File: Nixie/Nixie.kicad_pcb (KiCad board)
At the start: 2 copper layers, 41 parts, among them J1 Conn_01x05_Male, J2 USB_B_Micro, Q1 BC847, Q2 BC847, SW1 SW_Push, U1 K155ID1, U2 ESP-12E, U3 74HC595, U4 K155ID1, U5 K155ID1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

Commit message: Platinenlayout begonnen
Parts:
- moved C1 60.8 mm to (109.2, 65.8), turned to 90 degrees
- moved C7 60.2 mm to (147.7, 126.0), turned to -90 degrees
- moved H4 53.7 mm to (36.8, 49.5)
- moved U7 50.7 mm to (137.5, 120.9), turned to 90 degrees
- moved U4 50.5 mm to (110.5, 120.9), turned to 90 degrees
- moved U1 48.9 mm to (119.5, 70.9), turned to -90 degrees
- moved U5 48.7 mm to (146.5, 70.9), turned to -90 degrees
- moved U9 42.6 mm to (194.7, 93.1), turned to 90 degrees
- moved C10 31.0 mm to (209.1, 100.1)
- moved C5 24.3 mm to (120.7, 126.0), turned to -90 degrees
- moved C4 22.2 mm to (136.5, 65.8)
- moved U8 16.9 mm to (215.6, 92.2), turned to 180 degrees
- moved U3 15.0 mm to (81.5, 95.0), turned to 180 degrees
- moved C9 14.9 mm to (217.6, 100.1), turned to 180 degrees
- moved Q1 14.4 mm to (75.7, 86.2)
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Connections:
- J1 pad 1: /RX -> /TX
- J1 pad 2: /TX -> /RX
- J1 pad 3: /DTR -> /RTS
- J1 pad 4: /RTS -> /DTR
- U1 pad 12: (no net) -> GND
- U4 pad 12: (no net) -> GND
- U5 pad 12: (no net) -> GND
- U7 pad 12: (no net) -> GND
- U9 pad 3: GND -> 170V
- U9 pad 4: 170V -> GND
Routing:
- net Net-(U3-Pad5): track 0.00 -> 74.6 mm
- net Net-(U3-Pad6): track 0.00 -> 67.7 mm, vias 0 -> 1
- net Net-(U3-Pad7): track 0.00 -> 65.2 mm, vias 0 -> 1
- net Net-(U3-Pad15): track 0.00 -> 65.0 mm
- net RST: track 0.00 -> 63.5 mm, vias 0 -> 2
- net Net-(N4-Pad8): track 0.00 -> 60.0 mm
- net Net-(N4-Pad9): track 0.00 -> 57.7 mm, vias 0 -> 1
- net Net-(N3-Pad2): track 0.00 -> 56.3 mm
- net Net-(N2-Pad9): track 0.00 -> 56.1 mm
- net Net-(N1-Pad2): track 0.00 -> 55.3 mm
- net Net-(U3-Pad3): track 0.00 -> 54.9 mm, vias 0 -> 1
- net SER: track 0.00 -> 51.9 mm
- net Net-(N4-Pad0): track 0.00 -> 51.5 mm
- net Net-(N2-Pad8): track 0.00 -> 50.1 mm
- net RCLK: track 0.00 -> 50.0 mm
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
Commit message: PCB fertiggestellt
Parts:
- removed H1, H2: MountingHole_Pad, MountingHole:MountingHole_3.2mm_M3_Pad
- added ?: , , F.Cu at (184.0, 127.0)
- added H4: MountingHole_Pad, MountingHole:MountingHole_3.2mm_M3_Pad, F.Cu at (183.9, 59.9)
- C1, C2, C3, C4, C5, C6, C8: moved to B.Cu
- moved H3 193.9 mm to (64.7, 125.7)
- moved C10 44.3 mm to (169.3, 119.6)
- moved L1 44.3 mm to (169.3, 105.0)
- moved C9 44.3 mm to (177.9, 119.6)
- moved D1 44.3 mm to (174.4, 105.0)
- moved U8 44.3 mm to (175.9, 111.7)
- moved J2 43.4 mm to (186.3, 112.9)
- moved U9 33.1 mm to (167.6, 74.2), turned to 180 degrees
- moved H4 26.7 mm to (61.4, 59.9), turned to 90 degrees
- moved SW1 23.8 mm to (68.3, 103.2), turned to 0 degrees
- moved R2 17.7 mm to (61.5, 94.4)
- moved R1 16.9 mm to (61.8, 102.8), turned to -90 degrees
- moved U2 16.2 mm to (61.4, 81.5)
- moved R5 15.6 mm to (71.4, 70.8)
- moved C2 15.2 mm to (69.3, 95.7)
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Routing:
- net GND: track 13.7 -> 516.5 mm, vias 0 -> 8
- net +5V: track 18.7 -> 256.7 mm, vias 0 -> 3
- net +3.3V: track 17.3 -> 173.6 mm, vias 0 -> 2
- net SR_CLK: track 47.4 -> 198.2 mm, vias 0 -> 2
- net RCLK: track 50.0 -> 198.8 mm, vias 0 -> 2
- net Net-(U3-Pad9): track 0.00 -> 130.3 mm, vias 0 -> 2
- net Net-(U6-Pad7): track 0.00 -> 49.0 mm, vias 0 -> 1
- net Net-(U6-Pad2): track 0.00 -> 48.5 mm, vias 0 -> 1
- net Net-(U6-Pad4): track 0.00 -> 48.5 mm
- net Net-(U6-Pad1): track 0.00 -> 47.3 mm, vias 0 -> 1
- net Net-(U6-Pad3): track 0.00 -> 41.9 mm, vias 0 -> 1
- net Net-(U6-Pad5): track 0.00 -> 39.5 mm, vias 0 -> 1
- net Net-(U6-Pad15): track 0.00 -> 38.9 mm, vias 0 -> 1
- net Net-(U6-Pad6): track 0.00 -> 37.6 mm, vias 0 -> 1
- net Net-(N4-Pad4): track 43.0 -> 14.7 mm
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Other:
- board outline added: 132.3 x 76.6 mm
- copper layers 2 -> 4

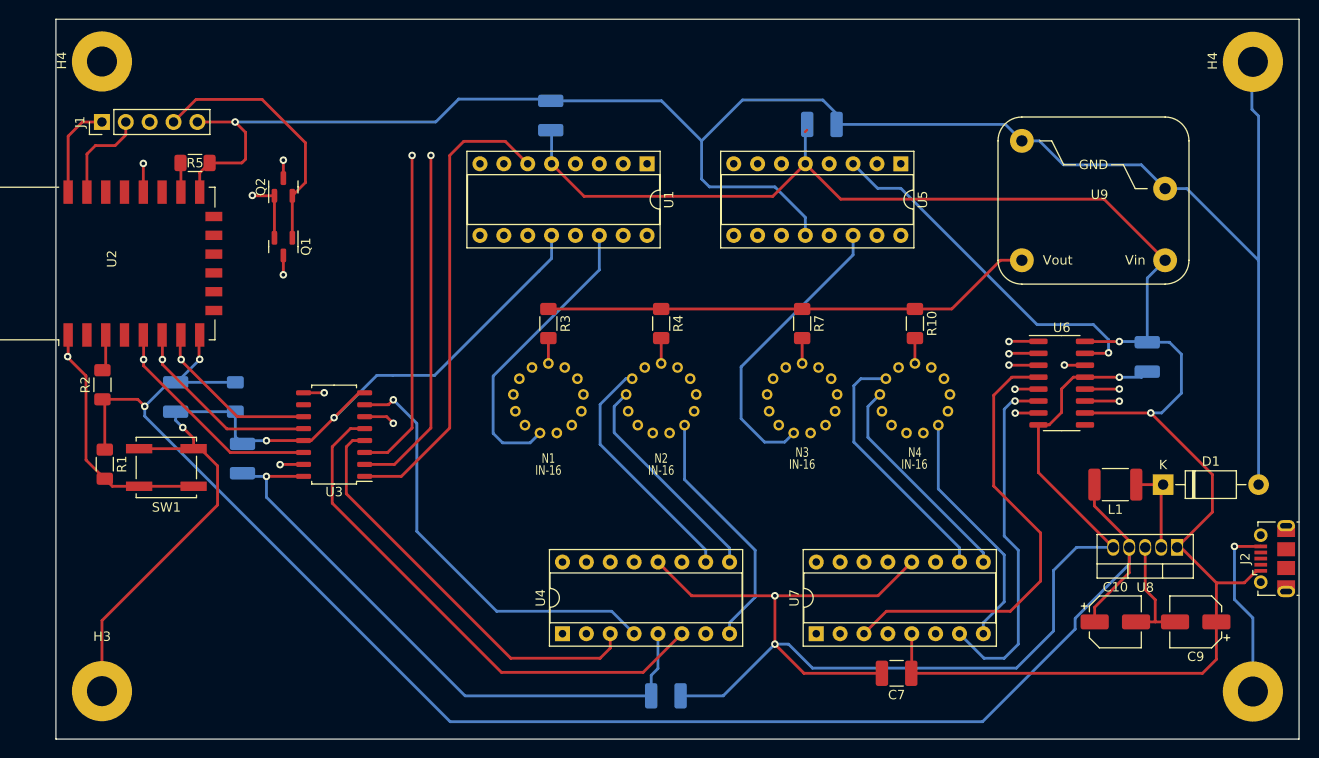
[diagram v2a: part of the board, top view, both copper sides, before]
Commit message: Added solid ground planes
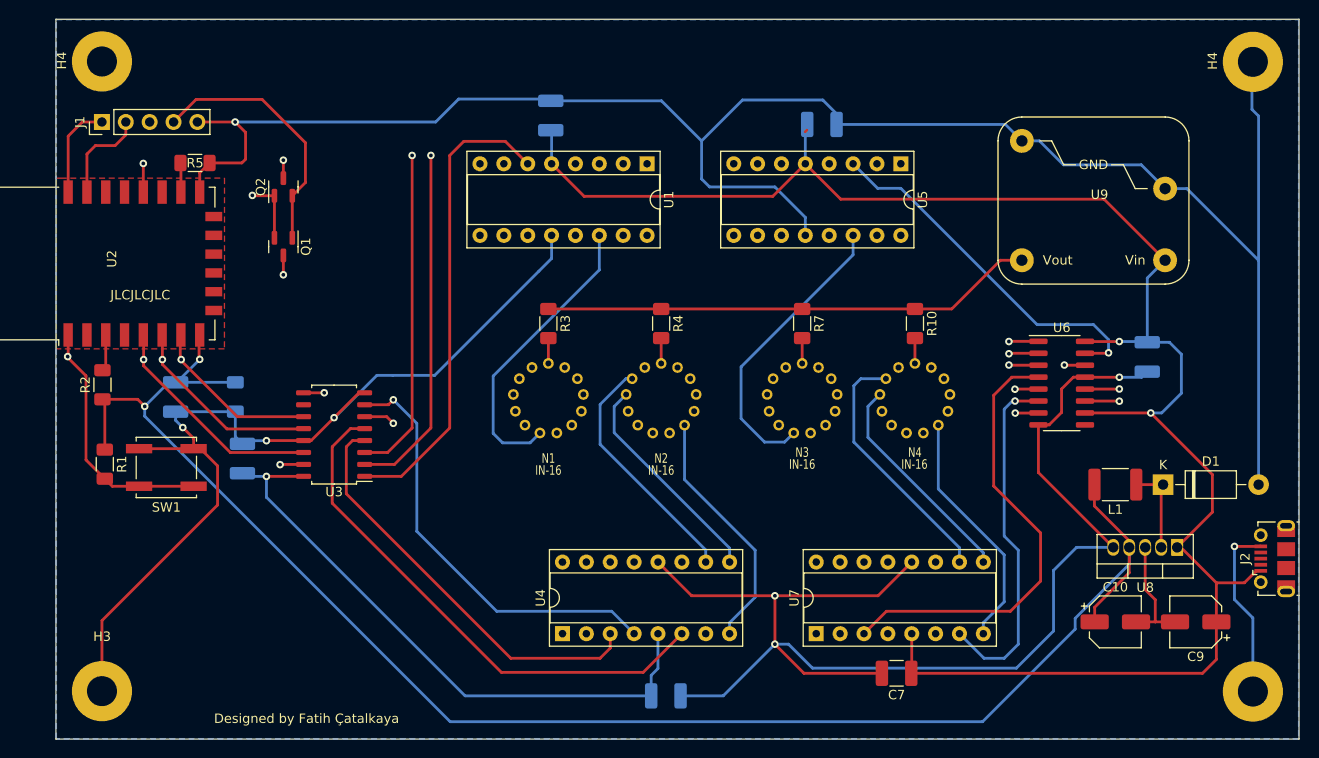
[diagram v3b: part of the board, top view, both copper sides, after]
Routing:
- added copper zone on B.Cu, net GND
- added copper zone on F.Cu, net GND
- added copper zone on In1.Cu, net GND
- added copper zone on In2.Cu, net GND
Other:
- board text added: "Designed by Fatih Çatalkaya"
- board text added: "JLCJLCJLC"
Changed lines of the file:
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@@
   )
   (gr_rect (start 56.6 55.51) (end 188.87 132.1) (layer "Edge.Cuts") (width 0.1) (fill none))
+  (gr_text "JLCJLCJLC\n" (at 65.58 84.85) (layer "F.SilkS")
+    (effects (font (size 1 1) (thickness 0.15)))
+  )
+  (gr_text "Designed by Fatih Çatalkaya" (at 83.27 129.92) (layer "F.SilkS")
+    (effects (font (size 1 1) (thickness 0.15)))
+  )
+  (dimension (type aligned) (layer "Cmts.User")
+    (pts (xy 188.87 55.51) (xy 188.87 132.1))
+    (height -5.13)
+    (gr_text "76.5900 mm" (at 192.85 93.805 90) (layer "Cmts.User")
+      (effects (font (size 1 1) (thickness 0.15)))
+    )
+    (format (units 3) (units_format 1) (precision 4))
+    (style (thickness 0.15) (arrow_length 1.27) (text_position_mode 0) (extension_height 0.58642) (extension_offset 0.5) keep_text_aligned)
+  )
+  (dimension (type aligned) (layer "Cmts.User")
+    (pts (xy 188.87 55.51) (xy 56.6 55.51))
+    (height 3.409999)
+    (gr_text "132.2700 mm" (at 122.735 50.950001) (layer "Cmts.User")
+      (effects (font (size 1 1) (thickness 0.15)))
+    )
+    (format (units 3) (units_format 1) (precision 4))
+    (style (thickness 0.15) (arrow_length 1.27) (text_position_mode 0) (extension_height 0.58642) (extension_offset 0.5) keep_text_aligned)
+  )
   (segment (start 179.65 107.95) (end 179.65 103.95) (width 0.3) (layer "F.Cu") (net 1))
   (segment (start 173.1 97.4) (end 166.095 97.4) (width 0.3) (layer "F.Cu") (net 1))
@@
   (segment (start 157.8 89.8) (end 158 89.8) (width 0.3) (layer "In2.Cu") (net 101))
   (segment (start 138.185 66.5) (end 149 66.5) (width 0.3) (layer "In2.Cu") (net 101))
+  (zone (net 2) (net_name "GND") (layers "F.Cu" "In1.Cu" "In2.Cu") (hatch edge 0.508)
+    (connect_pads (clearance 0.508))
+    (min_thickness 0.254) (filled_areas_thickness no)
+    (fill yes (thermal_gap 0.508) (thermal_bridge_width 0.508))
+    (polygon
+      (pts
+        (xy 74.53 90.58)
+        (xy 56.65 90.58)
+        (xy 56.65 72.42)
+        (xy 57.11 72.42)
+        (xy 74.54 72.41)
+      )
+    )
+  )
+  (zone (net 2) (net_name "GND") (layer "B.Cu") (hatch edge 0.508)
+    (connect_pads (clearance 0.508))
+    (min_thickness 0.254) (filled_areas_thickness no)
+    (fill yes (thermal_gap 0.508) (thermal_bridge_width 0.508))
+    (polygon
+      (pts
+        (xy 188.82 132.05)
+        (xy 56.65 132.05)
+        (xy 56.65 55.56)
+        (xy 188.82 55.56)
+      )
+    )
+  )
 )

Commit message: Kleinere Anpassungen
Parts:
- renumbered H4 to H2
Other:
- board text added: "12.07.2022"
- board text added: "DTR"
- board text added: "GND"
- board text added: "JLCJLCJLCJLC"
- board text added: "RTS"
- board text added: "RX"
- board text added: "TX"
- board text removed: "JLCJLCJLC"

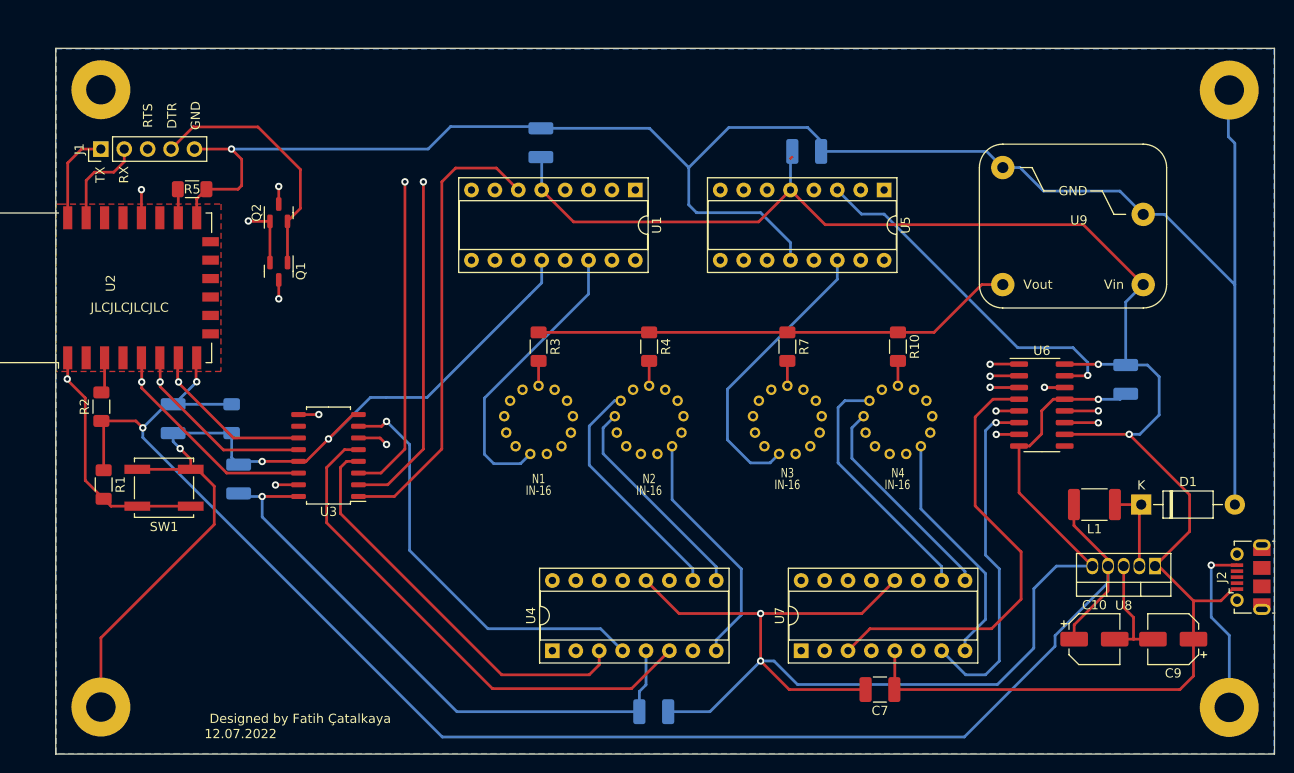
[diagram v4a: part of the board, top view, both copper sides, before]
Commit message: Designed 2-layer PCB
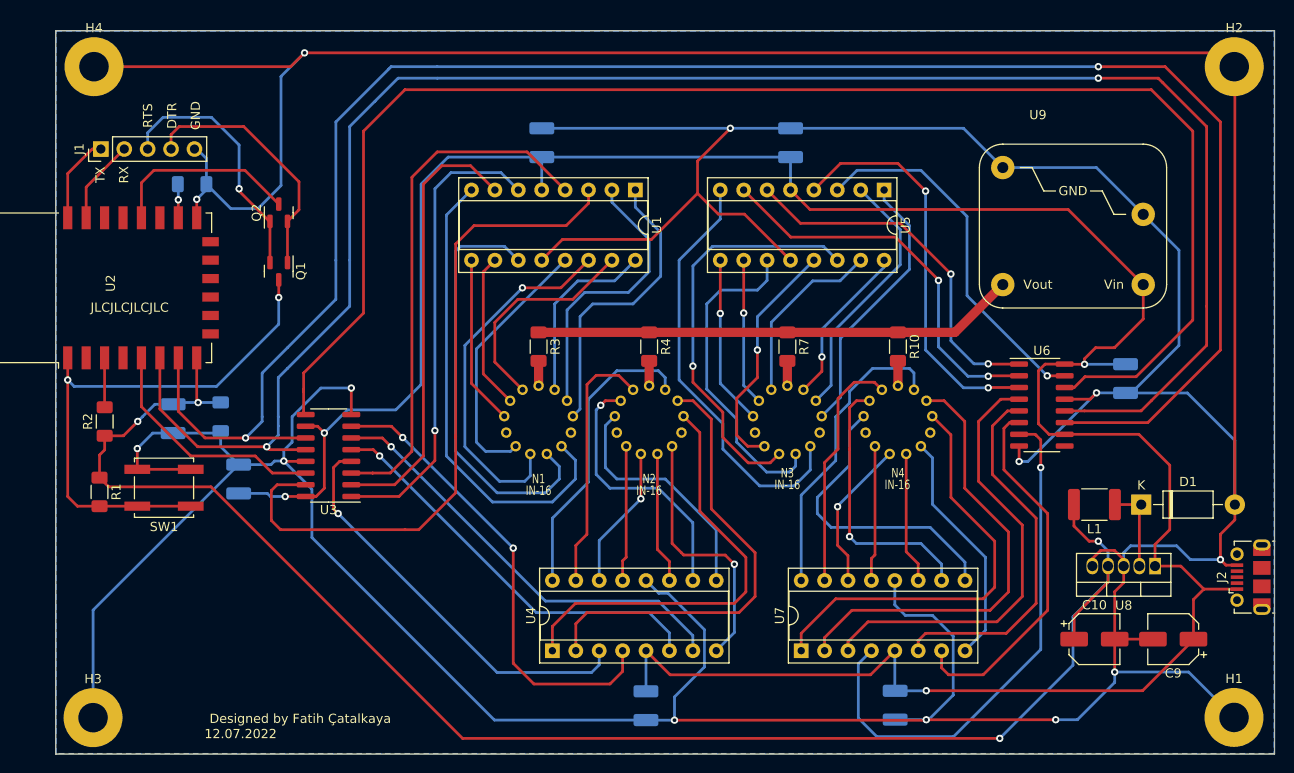
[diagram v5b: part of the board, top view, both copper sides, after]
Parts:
- removed ?: , 
- added H1: MountingHole_Pad, MountingHole:MountingHole_3.2mm_M3_Pad, F.Cu at (184.5, 128.1)
- C7, R5: moved to B.Cu
- U3: footprint Package_SO:SOIC-16_4.55x10.3mm_P1.27mm -> Package_SO:SOIC-16_3.9x9.9mm_P1.27mm
- U9: footprint nch_psu:NCH8200HV -> psu:NCH8200HV
- moved H3 4.73 mm to (60.6, 128.2)
- moved H2 2.52 mm to (184.5, 57.5), turned to 0 degrees
- moved H4 2.49 mm to (60.8, 57.5), turned to 0 degrees
- moved C7 2.37 mm to (147.7, 126.8), turned to -90 degrees
- moved C4 1.99 mm to (136.3, 65.8), turned to 90 degrees
- moved R2 1.65 mm to (61.9, 96.0)
- moved C8 1.21 mm to (74.5, 95.5)
- moved C5 1.07 mm to (120.7, 126.8), turned to -90 degrees
- moved R1 0.92 mm to (61.4, 103.7)
- moved R5 0.55 mm to (71.4, 70.2)
- moved C1 0.10 mm to (109.3, 65.8)
- moved C6 0.09 mm to (172.7, 91.3)
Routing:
- net GND: track 516.5 -> 671.6 mm, vias 8 -> 13
- net Net-(U3-Pad9): track 130.3 -> 165.0 mm, vias 2 -> 0
- net +5V: track 256.7 -> 287.8 mm, vias 3 -> 4
- net Net-(N3-Pad5): track 31.5 -> 44.8 mm, vias 0 -> 1
- net Net-(N1-Pad6): track 33.6 -> 46.4 mm
- net Net-(U3-Pad5): track 56.6 -> 44.7 mm, vias 0 -> 1
- net Net-(N4-Pad3): track 23.4 -> 32.8 mm
- net Net-(U3-Pad6): track 56.6 -> 47.6 mm
- net Net-(U6-Pad7): track 49.0 -> 57.8 mm
- net Net-(N1-Pad5): track 31.6 -> 39.5 mm, vias 0 -> 1
- net Net-(U5-Pad6): track 47.3 -> 39.4 mm, vias 1 -> 2
- net Net-(U1-Pad3): track 67.2 -> 74.3 mm, vias 1 -> 0
- net SR_CLK: track 198.2 -> 205.1 mm
- net Net-(U5-Pad7): track 48.5 -> 42.5 mm, vias 1 -> 2
- net Net-(N1-Pad1): track 18.1 -> 24.1 mm
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- removed copper zone on F.Cu, net GND
- removed copper zone on In1.Cu, net GND
- removed copper zone on In2.Cu, net GND
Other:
- board size 132.3 x 76.6 mm -> 132.3 x 78.5 mm
- copper layers 4 -> 2

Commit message: Smaller Adjustments
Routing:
- net GND: track 671.6 -> 672.6 mm
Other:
- board text added: "17.07.2022"
- board text removed: "12.07.2022"
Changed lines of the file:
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@@
     (effects (font (size 1 1) (thickness 0.15)))
   )
-  (gr_text "12.07.2022" (at 76.66 129.91) (layer "F.SilkS")
+  (gr_text "17.07.2022" (at 76.66 129.91) (layer "F.SilkS")
     (effects (font (size 1 1) (thickness 0.15)))
   )
@@
   (segment (start 88.675 92.375) (end 88.675 95.255) (width 0.3) (layer "F.Cu") (net 2))
   (segment (start 71.9 71.9) (end 71.9 73.9) (width 0.3) (layer "F.Cu") (net 2))
-  (segment (start 82.1 57.5) (end 60.75 57.5) (width 0.3) (layer "F.Cu") (net 2))
   (segment (start 83.725 100.335) (end 81.385 100.335) (width 0.3) (layer "F.Cu") (net 2))
   (segment (start 172.5 113.5) (end 171.525 114.475) (width 0.3) (layer "F.Cu") (net 2))
@@
   (segment (start 111.595 76.25) (end 121.25 76.25) (width 0.3) (layer "F.Cu") (net 2))
   (segment (start 65.45 98.95) (end 65.45 101.2) (width 0.3) (layer "F.Cu") (net 2))
-  (segment (start 83.6 56) (end 82.1 57.5) (width 0.3) (layer "F.Cu") (net 2))
   (segment (start 170 110) (end 171.5 110) (width 0.3) (layer "F.Cu") (net 2))
   (segment (start 169.55 92.9) (end 168.86 93.59) (width 0.3) (layer "F.Cu") (net 2))
@@
   (segment (start 129.8125 64.1875) (end 136.35 64.1875) (width 0.3) (layer "B.Cu") (net 2))
   (segment (start 109.35 64.1875) (end 129.8125 64.1875) (width 0.3) (layer "B.Cu") (net 2))
+  (segment (start 82.375 54.775) (end 83.6 56) (width 0.3) (layer "B.Cu") (net 2))
   (segment (start 184.565 105.025) (end 184.565 98.065) (width 0.3) (layer "B.Cu") (net 2))
   (segment (start 151.075 128.375) (end 147.7125 128.375) (width 0.3) (layer "B.Cu") (net 2))
@@
   (segment (start 76.4375 100.6875) (end 60.65 116.475) (width 0.3) (layer "B.Cu") (net 2))
   (segment (start 127 122.65) (end 123.75 125.9) (width 0.3) (layer "B.Cu") (net 2))
+  (segment (start 63.475 54.775) (end 82.375 54.775) (width 0.3) (layer "B.Cu") (net 2))
   (segment (start 80.35 100.3) (end 79.9625 100.6875) (width 0.3) (layer "B.Cu") (net 2))
+  (segment (start 60.75 57.5) (end 63.475 54.775) (width 0.3) (layer "B.Cu") (net 2))
   (segment (start 74.2975 97.265) (end 74.5 97.0625) (width 0.3) (layer "B.Cu") (net 2))
   (segment (start 83.6 56) (end 81.05 58.55) (width 0.3) (layer "B.Cu") (net 2))
